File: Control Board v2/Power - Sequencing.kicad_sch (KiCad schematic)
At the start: 0 parts

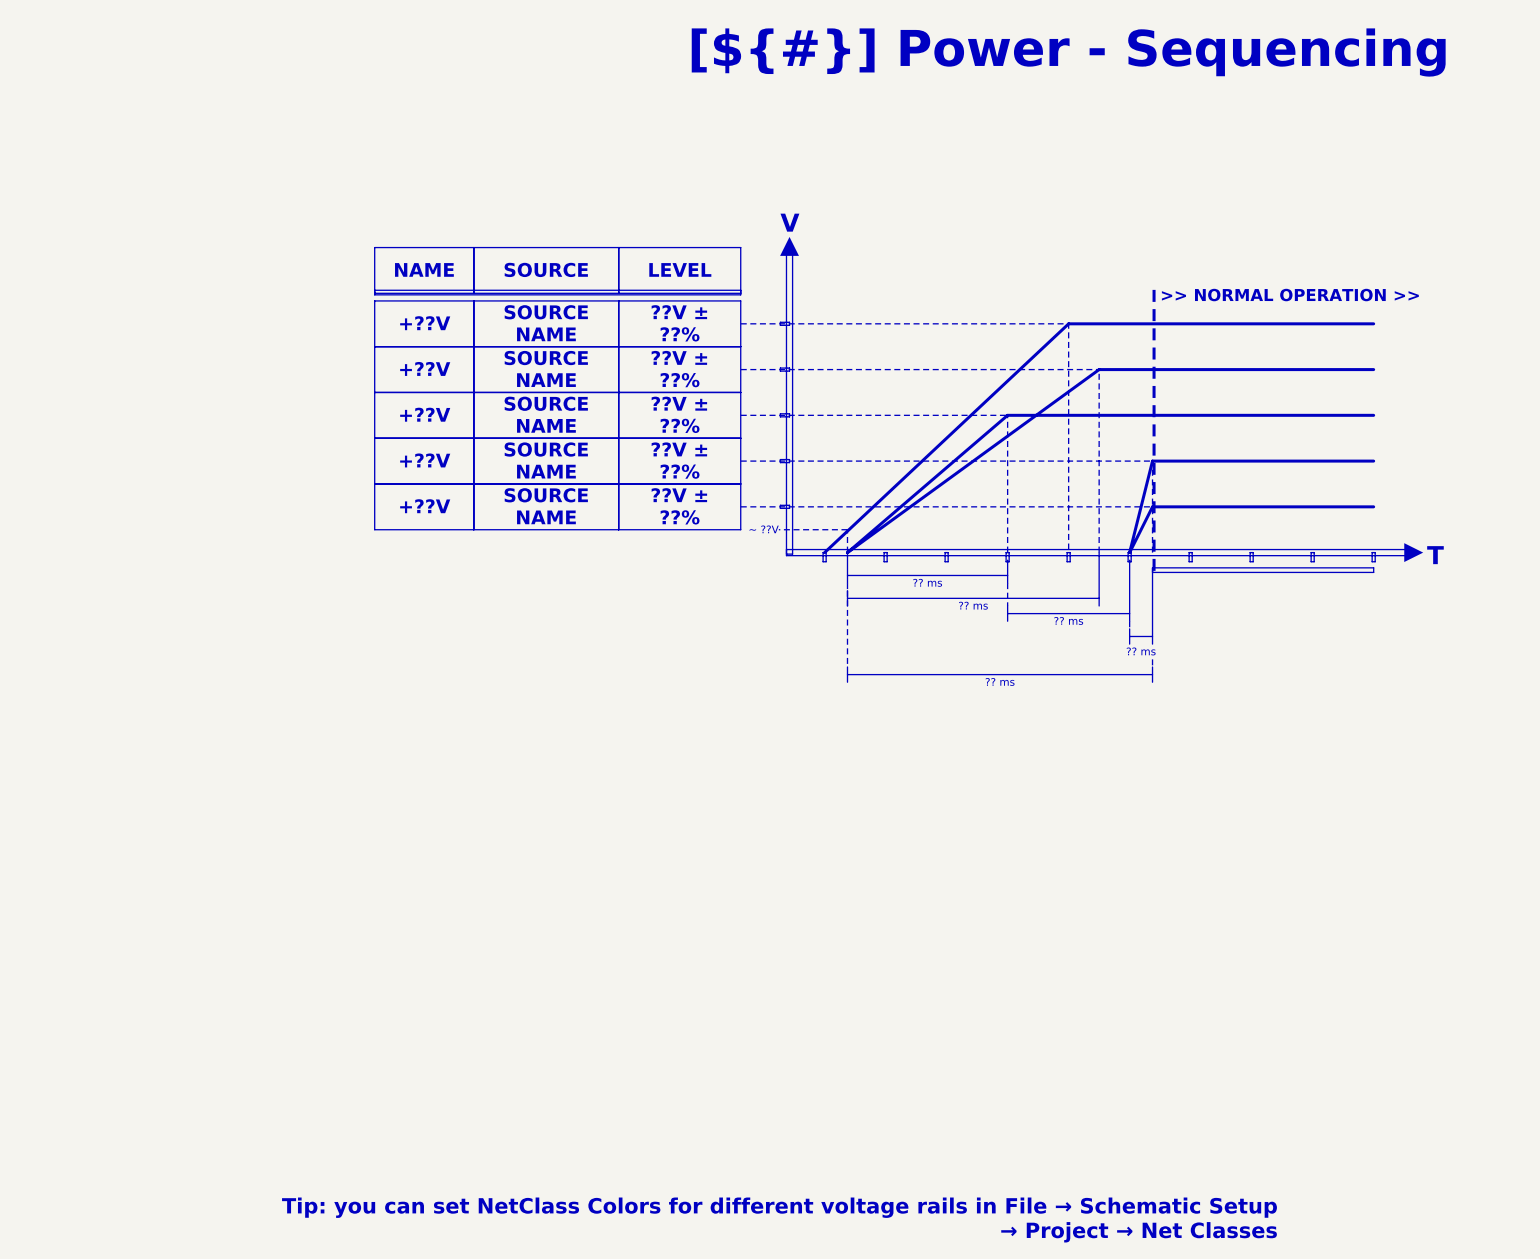
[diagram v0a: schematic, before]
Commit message: Finish preparing the template for v2 design
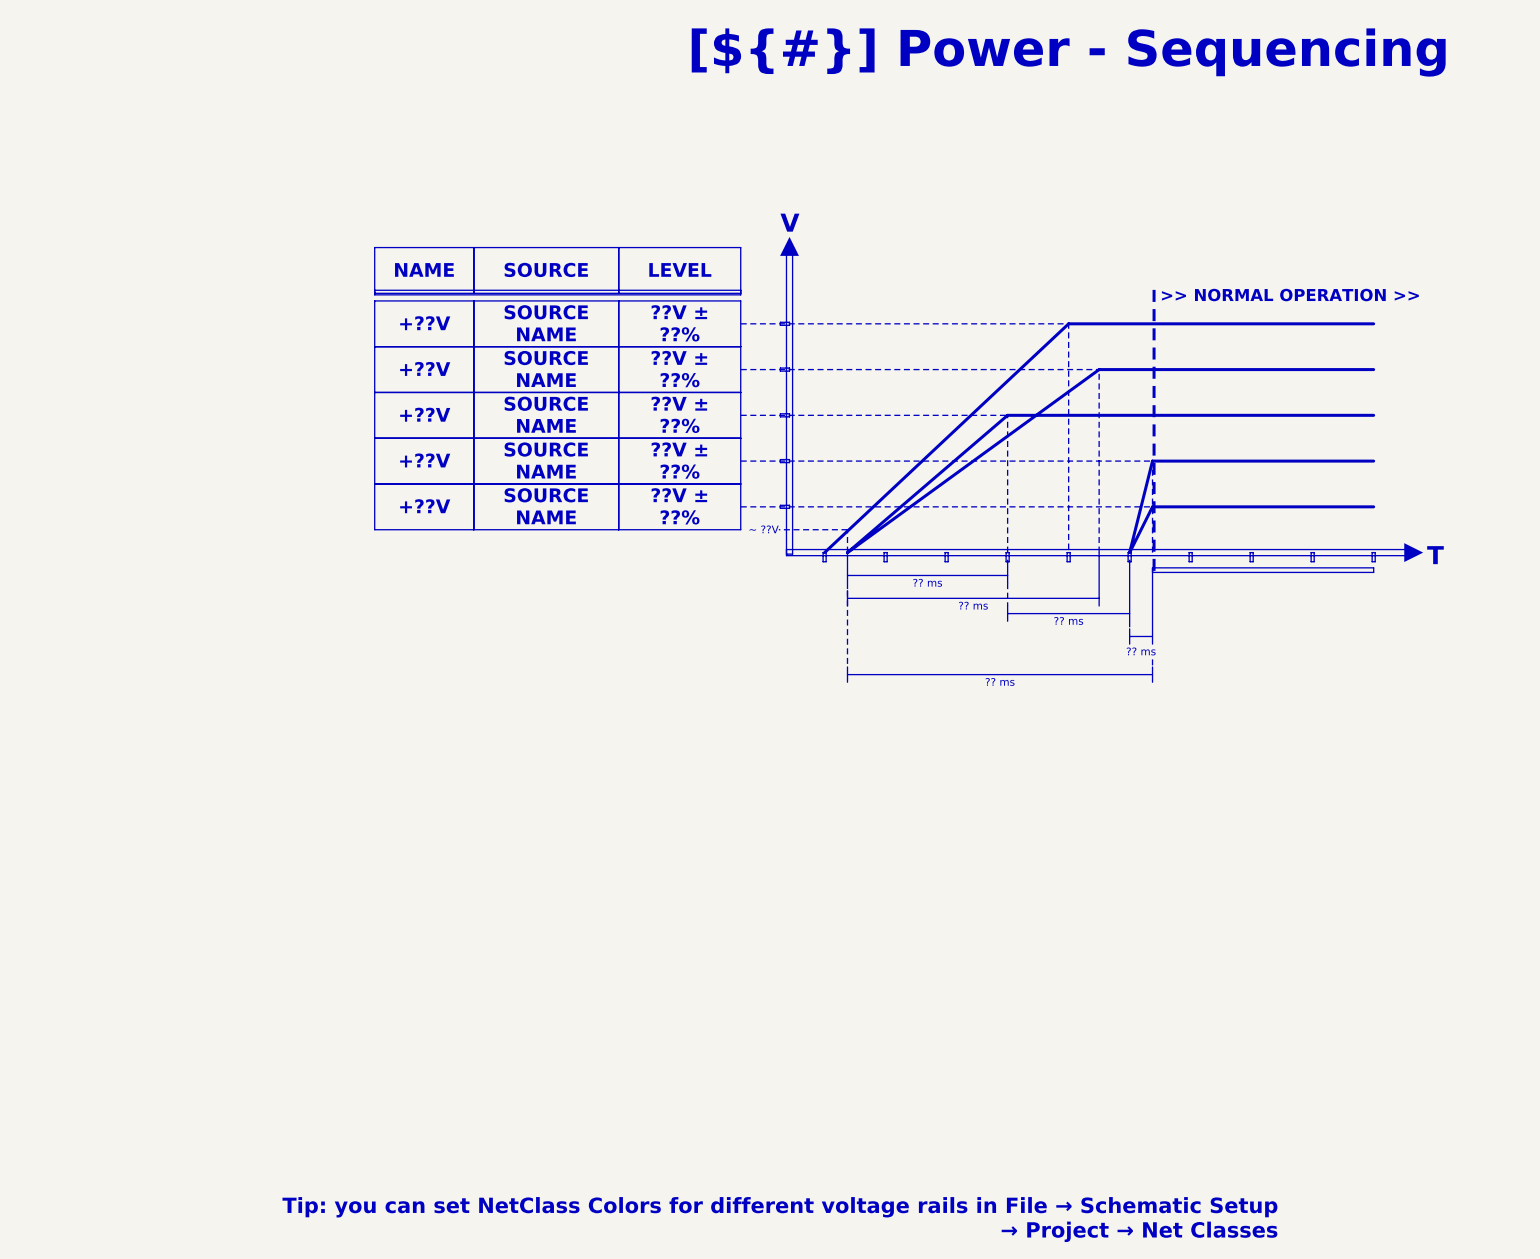
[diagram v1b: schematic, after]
